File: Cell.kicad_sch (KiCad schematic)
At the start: 19 parts

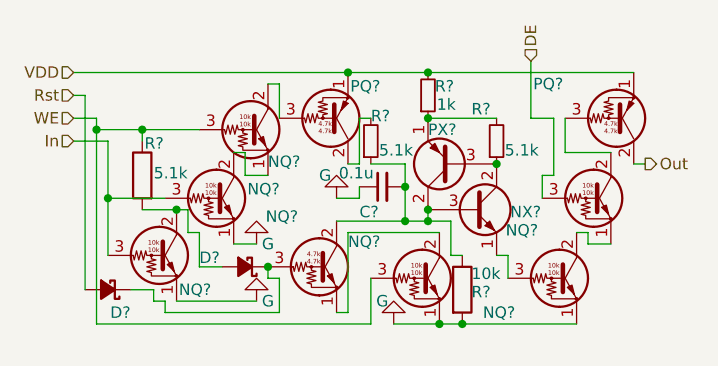
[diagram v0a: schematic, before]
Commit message: Schematics with 'sub-schematics' almost done
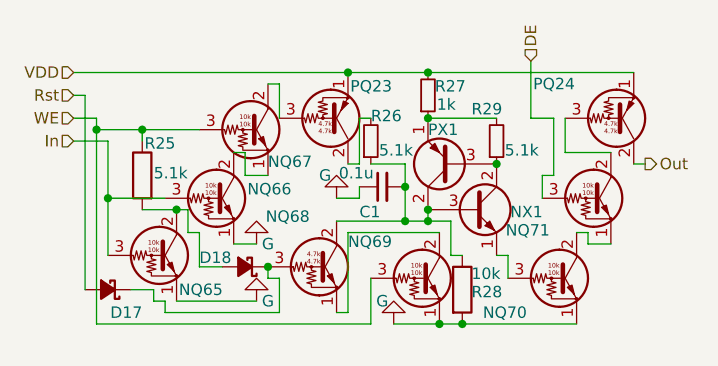
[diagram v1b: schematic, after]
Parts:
- gave numbers to parts that had none: 19

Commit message: Editing PCB, 1 cell temp-done
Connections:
- net G renamed GND
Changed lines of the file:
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@@
 			)
 		)
-		(property "Value" "G"
-			(at 52.07 45.72 0)
+		(property "Value" "GND"
+			(at 53.34 49.53 0)
 			(effects
 				(font
@@
 			)
 		)
-		(property "Value" "G"
-			(at 45.72 31.75 0)
+		(property "Value" "GND"
+			(at 46.99 35.306 0)
 			(effects
 				(font
@@
 			)
 		)
-		(property "Value" "G"
-			(at 39.37 45.72 0)
+		(property "Value" "GND"
+			(at 42.672 46.228 0)
 			(effects
 				(font
@@
 			)
 		)
-		(property "Value" "G"
-			(at 39.37 39.37 0)
+		(property "Value" "GND"
+			(at 40.386 39.116 0)
 			(effects
 				(font
